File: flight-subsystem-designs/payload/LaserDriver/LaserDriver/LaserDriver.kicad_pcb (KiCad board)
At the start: 4 copper layers, 50.5 x 50 mm, 40 parts, among them J1 Signal In, J2 Laser 0, J3 Laser 1, J5 VIN, U1 74LVC1G04, U2 SY100ELT22ZG-TR, U3 MAX3967AETG+, U4 MAX3967AETG+, U5 LDL212PV33R

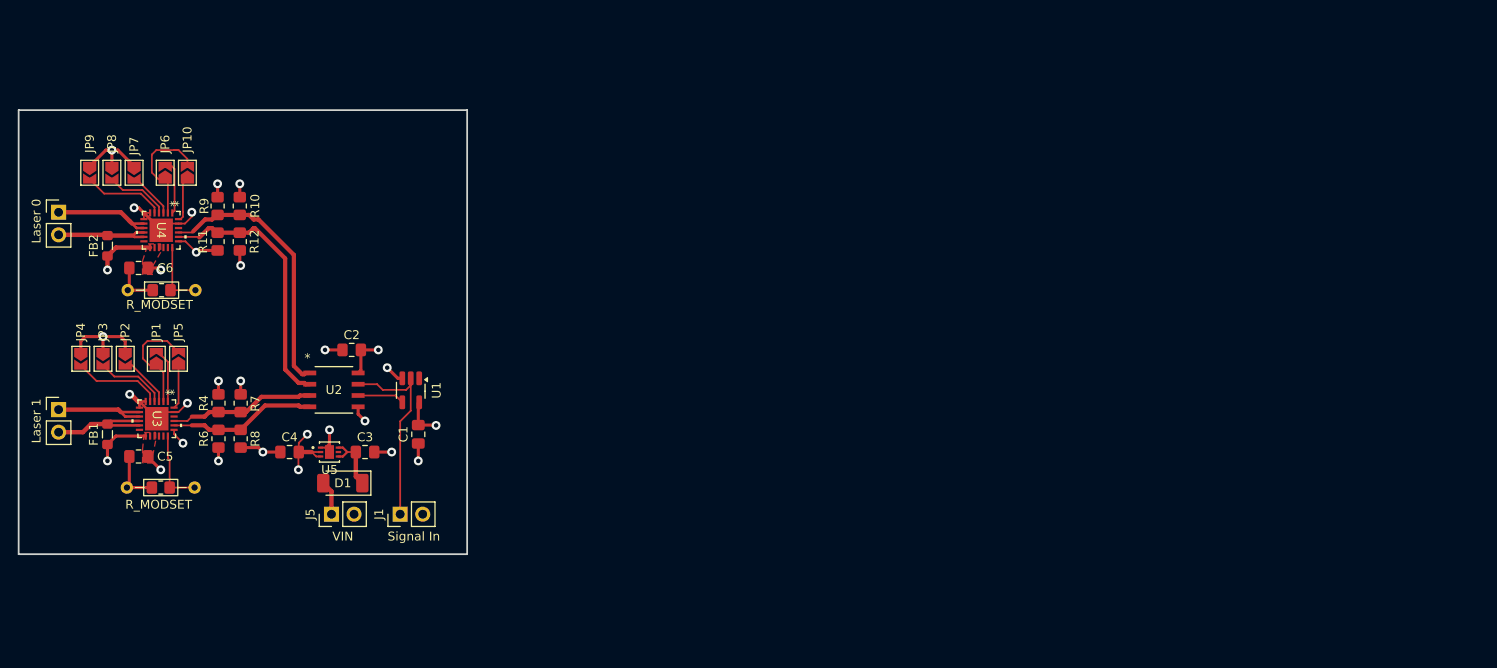
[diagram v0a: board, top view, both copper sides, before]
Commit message: laserdriver: add bnc and mounting holes
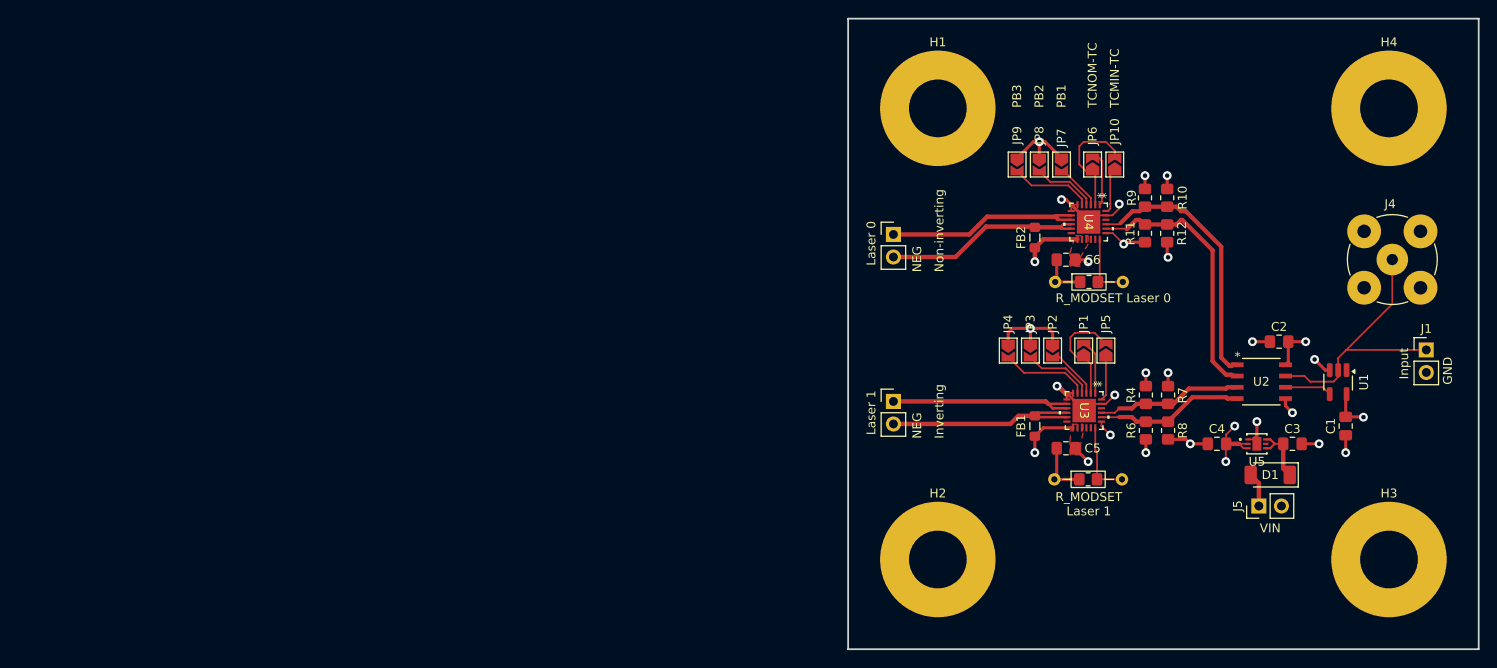
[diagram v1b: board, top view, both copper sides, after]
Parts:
- added H1: MountingHole_Pad, MountingHole:MountingHole_6.5mm_Pad, F.Cu at (127.0, 50.8)
- added H2: MountingHole_Pad, MountingHole:MountingHole_6.5mm_Pad, F.Cu at (127.0, 101.6)
- added H3: MountingHole_Pad, MountingHole:MountingHole_6.5mm_Pad, F.Cu at (177.8, 101.6)
- added H4: MountingHole_Pad, MountingHole:MountingHole_6.5mm_Pad, F.Cu at (177.8, 50.8)
- added J4: BNC, Connector_Coaxial:BNC_TEConnectivity_1478204_Vertical, F.Cu at (178.2, 67.8)
- J1: value Signal In -> Input
- moved J1 117.0 mm to (182.0, 78.0), turned to 0 degrees
- moved C1 104.4 mm to (172.9, 86.6)
- moved C2 104.4 mm to (165.4, 77.1)
- moved C3 104.4 mm to (166.9, 88.6)
- moved C4 104.4 mm to (158.4, 88.6)
- moved C5 104.4 mm to (141.4, 89.1)
- moved C6 104.4 mm to (141.4, 67.8)
- moved D1 104.4 mm to (164.4, 92.1)
- moved FB1 104.4 mm to (137.9, 86.6)
- moved FB2 104.4 mm to (137.9, 65.3)
- moved J5 104.4 mm to (163.2, 95.6)
- moved JP1 104.4 mm to (143.4, 78.1)
- moved JP10 104.4 mm to (146.9, 57.1)
- moved JP2 104.4 mm to (139.9, 78.1)
- moved JP3 104.4 mm to (137.4, 78.1)
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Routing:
- net /Laser0_PWR_N: track 11.1 -> 22.9 mm
- net /Laser0_PWR_P: track 12.1 -> 22.8 mm
- net /Laser1_PWR_N: track 13.3 -> 23.7 mm
- net /Laser1_PWR_P: track 11.5 -> 22.0 mm
- net /SIGNAL_IN: track 22.5 -> 31.2 mm
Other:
- board size 50.5 x 50 mm -> 71 x 71 mm
- board text added: "GND"
- board text added: "Inverting"
- board text added: "NEG"
- board text added: "Non-inverting"
- board text added: "PB1"
- board text added: "PB2"
- board text added: "PB3"
- board text added: "R_MODSET Laser 0"
- board text added: "R_MODSET Laser 1"
- board text added: "TCMIN-TC"
- board text added: "TCNOM-TC"
- board text removed: "R_MODSET"

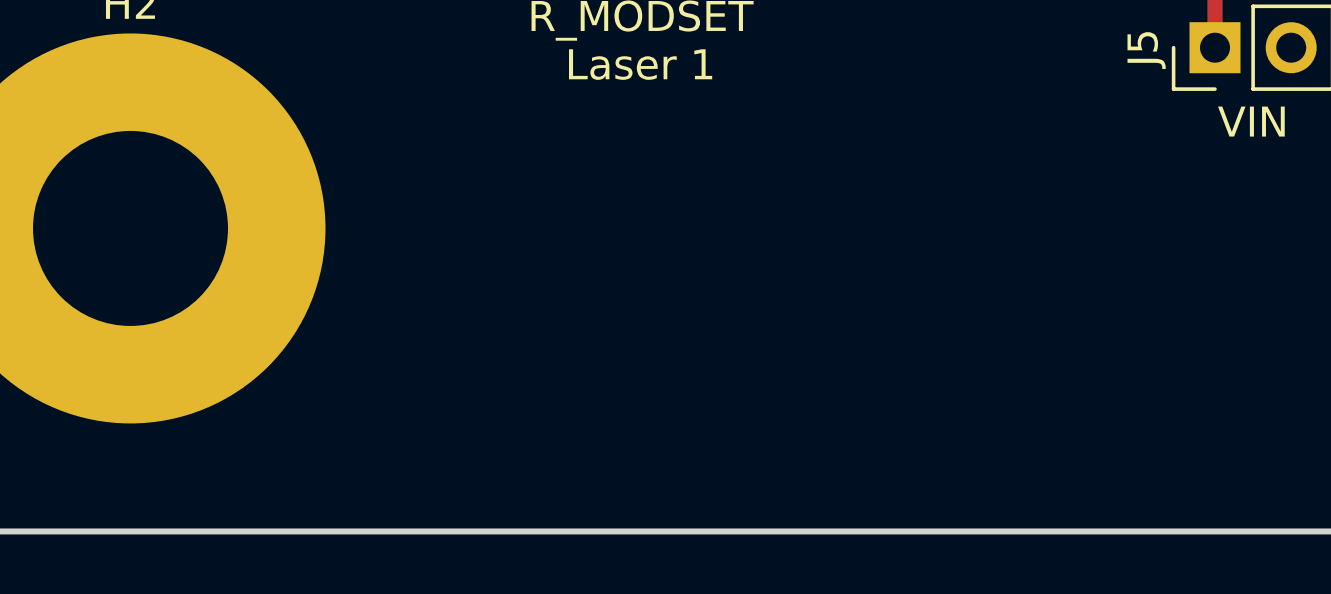
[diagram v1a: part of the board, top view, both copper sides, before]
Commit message: feat: PDU updates and laser driver v1.0.1
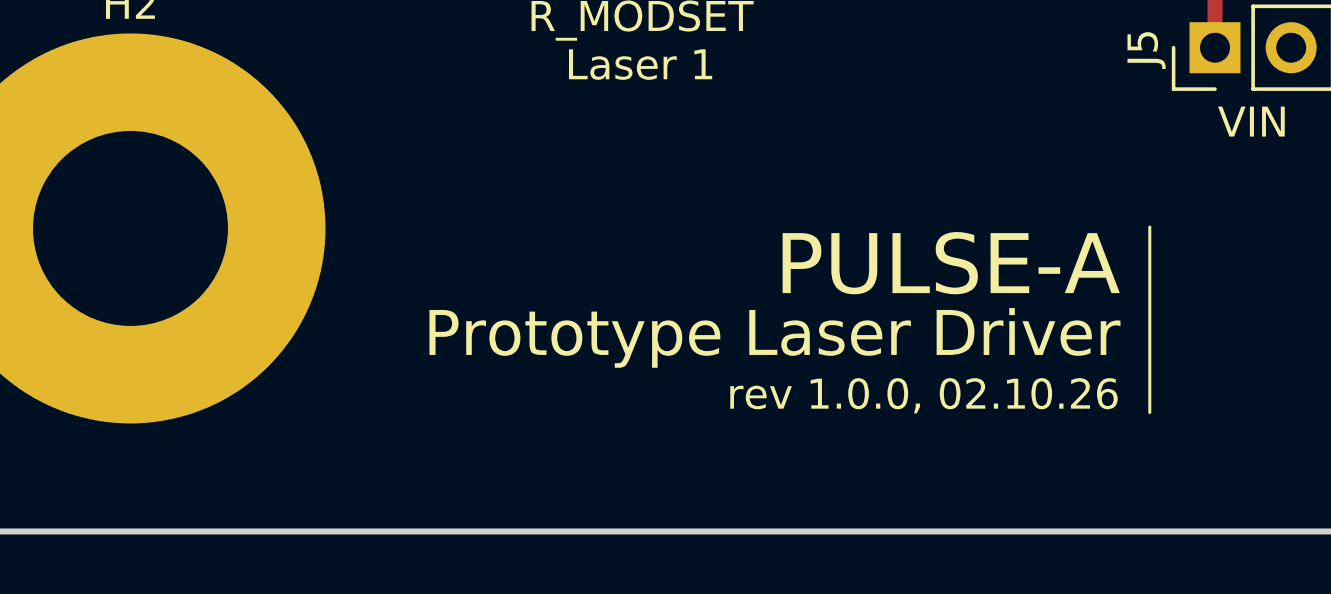
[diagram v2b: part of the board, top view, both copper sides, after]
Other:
- board text added: "PULSE-A"
- board text added: "Prototype Laser Driver"
- board text added: "rev 1.0.0, 02.10.26"

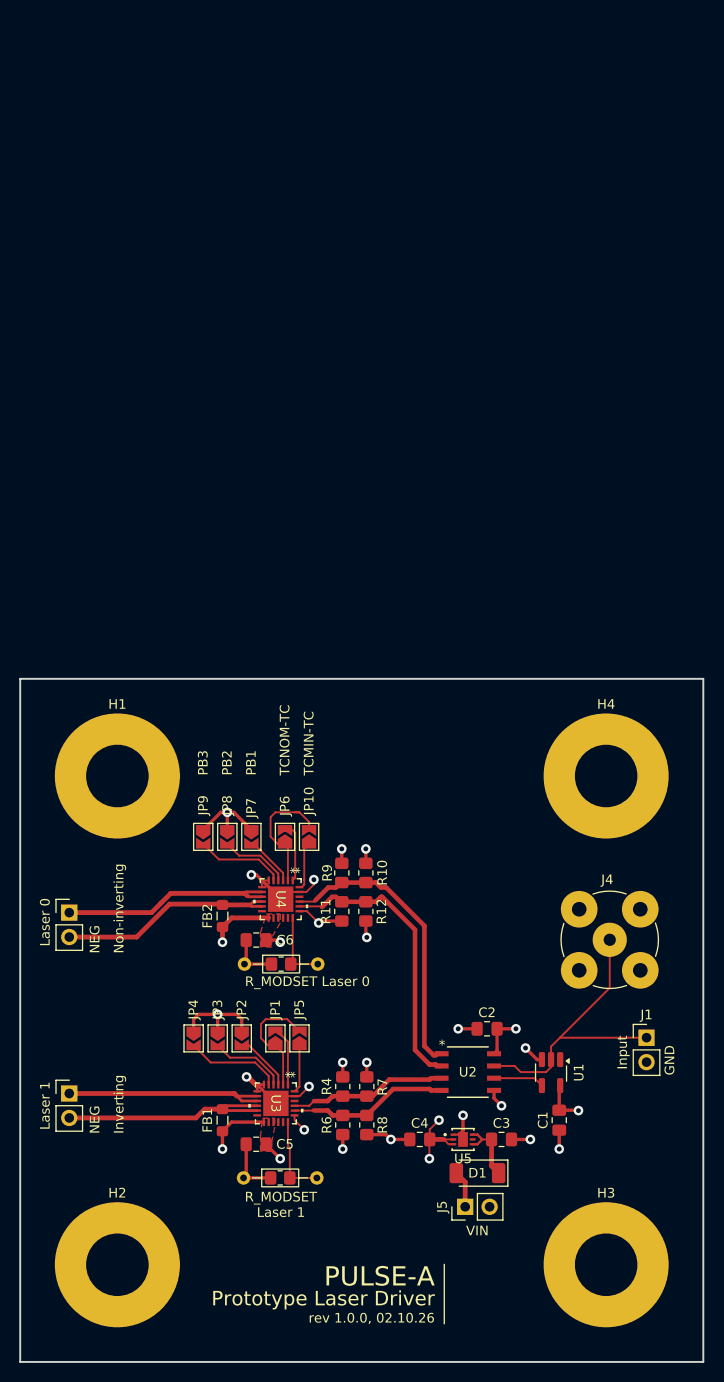
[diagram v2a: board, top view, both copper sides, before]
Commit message: laserdriver: reset all annotations and cleared pcb :sob:
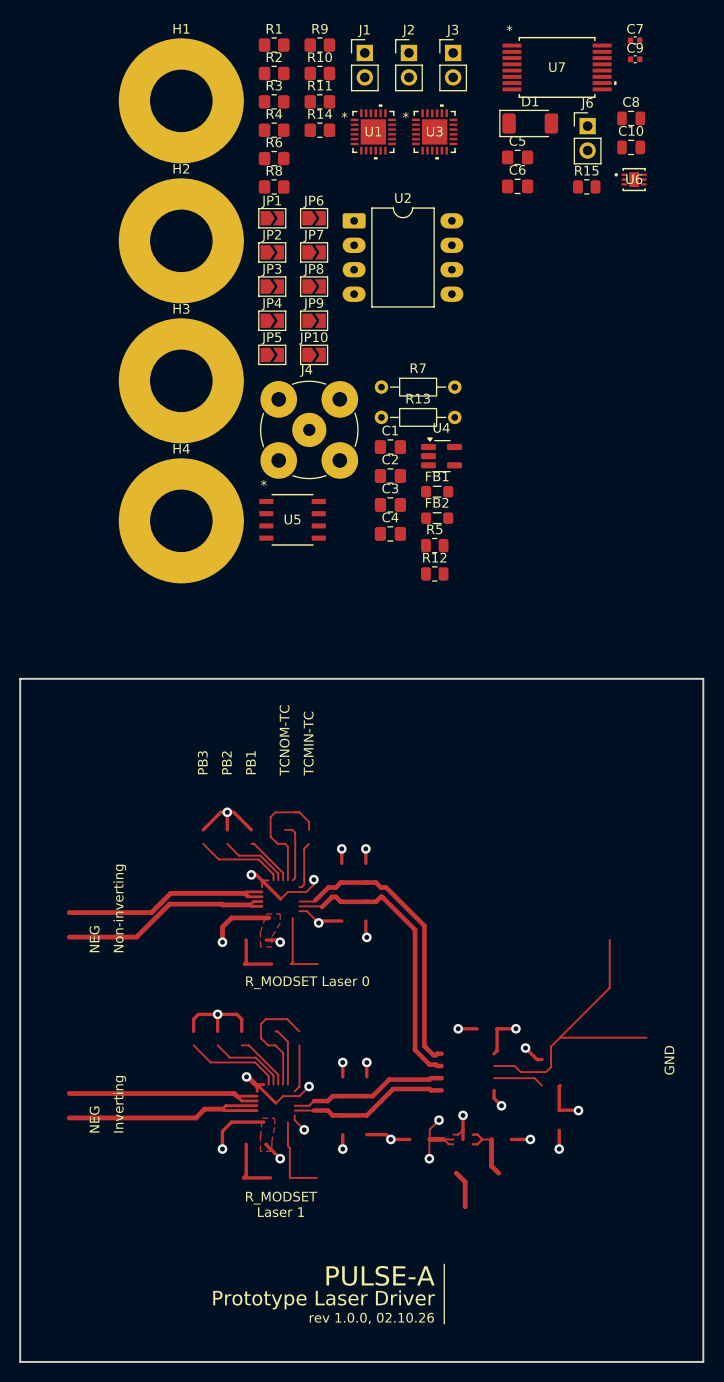
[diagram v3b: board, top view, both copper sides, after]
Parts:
- removed J5: VIN, Connector_PinHeader_2.54mm:PinHeader_1x02_P2.54mm_Vertical
- added C10: 22uF, Capacitor_SMD:C_0805_2012Metric, F.Cu at (180.4, -14.5)
- added C7: 15nF, Capacitor_SMD:C_0402_1005Metric, F.Cu at (180.8, -25.7)
- added C8: 10uF, Capacitor_SMD:C_0805_2012Metric, F.Cu at (180.4, -17.5)
- added C9: 15nF, Capacitor_SMD:C_0402_1005Metric, F.Cu at (180.8, -23.7)
- added J6: VIN Pin Header, Connector_PinHeader_2.54mm:PinHeader_1x02_P2.54mm_Vertical, F.Cu at (175.9, -16.8)
- added R13: R_MODSET, Resistor_THT:R_Axial_DIN0204_L3.6mm_D1.6mm_P7.62mm_Horizontal, F.Cu at (154.4, 13.5)
- added R14: R_MODSET, Resistor_SMD:R_0805_2012Metric_Pad1.20x1.40mm_HandSolder, F.Cu at (148.0, -16.3)
- added R15: 18k, Resistor_SMD:R_0805_2012Metric, F.Cu at (175.8, -10.4)
- added U6: LDL212PV33R, footprints:DFN_V33R_STM, F.Cu at (180.7, -11.2)
- added U7: UCC33420RAQR, footprints:SSOP16_DHA_TEX, F.Cu at (172.7, -22.8)
- C3: value 1uF -> 0.1uF
- C4: value 4.7uF -> 0.1uF
- C5: value 0.1uF -> 4.7uF
- C6: value 0.1uF -> 1uF
- J1: value Input -> Laser 0
- J2: value Laser 0 -> Laser 1
- J3: value Laser 1 -> Input
- R1: value R_MODSET -> 130; footprint Resistor_THT:R_Axial_DIN0204_L3.6mm_D1.6mm_P7.62mm_Horizontal -> Resistor_SMD:R_0805_2012Metric_Pad1.20x1.40mm_HandSolder
- R10, R8: value 83 -> 130
- R11, R4, R9: value 130 -> 83
- R12: value 83 -> 10k; footprint Resistor_SMD:R_0805_2012Metric_Pad1.20x1.40mm_HandSolder -> Resistor_SMD:R_0805_2012Metric
- R2: value R_MODSET -> 83; footprint Resistor_THT:R_Axial_DIN0204_L3.6mm_D1.6mm_P7.62mm_Horizontal -> Resistor_SMD:R_0805_2012Metric_Pad1.20x1.40mm_HandSolder
- R3: value R_MODSET -> 130
- R5: value R_MODSET -> 360; footprint Resistor_SMD:R_0805_2012Metric_Pad1.20x1.40mm_HandSolder -> Resistor_SMD:R_0805_2012Metric
- R6: value 130 -> R_MODSET
- R7: value 83 -> R_MODSET; footprint Resistor_SMD:R_0805_2012Metric_Pad1.20x1.40mm_HandSolder -> Resistor_THT:R_Axial_DIN0204_L3.6mm_D1.6mm_P7.62mm_Horizontal
- U1: value 74LVC1G04 -> MAX3967AETG+; footprint Package_TO_SOT_SMD:SOT-23-5_HandSoldering -> footprints:21-0139_T2444&plus_4_MXM
- U2: value SY100ELT22ZG-TR -> DPC6137; footprint footprints:SOIC-8_M_MCH -> Package_DIP:DIP-8_W10.16mm_LongPads
- U4: value MAX3967AETG+ -> 74LVC1G04; footprint footprints:21-0139_T2444&plus_4_MXM -> Package_TO_SOT_SMD:SOT-23-5_HandSoldering
- U5: value LDL212PV33R -> SY100ELT22ZG-TR; footprint footprints:DFN_V33R_STM -> footprints:SOIC-8_M_MCH
- moved R1 117.8 mm to (143.3, -25.2)
- moved J3 115.3 mm to (161.9, -24.4)
- moved D1 109.2 mm to (169.9, -17.0), turned to 0 degrees
- moved H2 106.6 mm to (133.6, -4.82)
- moved J1 106.5 mm to (152.7, -24.4)
- moved C5 106.1 mm to (168.6, -13.5), turned to 0 degrees
- moved U3 102.3 mm to (160.0, -16.1), turned to 0 degrees
- moved H3 101.9 mm to (133.6, 9.73)
- moved R6 100.7 mm to (143.3, -13.4), turned to 0 degrees
- moved R4 99.7 mm to (143.3, -16.3), turned to 0 degrees
- moved U1 99.5 mm to (153.6, -16.1), turned to 0 degrees
- moved R8 98.0 mm to (143.3, -10.4), turned to 0 degrees
- moved J2 96.1 mm to (157.3, -24.4)
- moved R2 92.6 mm to (143.3, -22.2)
- moved R3 89.6 mm to (143.3, -19.3)
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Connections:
- C1 pad 1: GND -> +3V3
- C1 pad 2: +3V3 -> GND
- C3 pad 1: /VIN -> +3V3
- C6 pad 1: +3V3 -> +5V
- D1 pad 1: /VIN -> /Power Input and Filtering/VIN
- J1 pad 1: /SIGNAL_IN -> /Laser0_PWR_P
- J1 pad 2: GND -> /Laser0_PWR_N
- J2 pad 1: /Laser0_PWR_P -> /Laser1_PWR_P
- J2 pad 2: /Laser0_PWR_N -> /Laser1_PWR_N
- J3 pad 1: /Laser1_PWR_P -> /SIGNAL_IN
- J3 pad 2: /Laser1_PWR_N -> GND
- JP10 pad 1: Net-(JP10-A) -> GND
- JP2 pad 1: GND -> Net-(JP1-A)
- JP5 pad 1: Net-(JP5-A) -> GND
- JP5 pad 2: Net-(JP1-A) -> Net-(JP5-B)
- JP6 pad 1: Net-(JP10-B) -> Net-(JP6-A)
- JP7 pad 1: GND -> Net-(JP6-A)
- R1 pad 1: GND -> +3V3
- R1 pad 2: Net-(U3-MODSET) -> /Laser1_PECL_P
- R10 pad 1: /Laser0_PECL_P -> +3V3
- R10 pad 2: GND -> /Laser0_PECL_N
- R11 pad 1: +3V3 -> /Laser0_PECL_N
- R11 pad 2: /Laser0_PECL_N -> GND
- R12 pad 1: /Laser0_PECL_N -> /ISO_SIGNAL_IN
- R12 pad 2: GND -> +5V
- R2 pad 1: GND -> /Laser1_PECL_P
- R2 pad 2: Net-(U4-MODSET) -> GND
- R3 pad 1: GND -> +3V3
- R3 pad 2: Net-(U4-MODSET) -> /Laser1_PECL_N
- R4 pad 1: +3V3 -> /Laser1_PECL_N
- R4 pad 2: /Laser1_PECL_P -> GND
- R5 pad 2: Net-(U3-MODSET) -> Net-(U2-Cathode)
- R6 pad 1: +3V3 -> Net-(U1-MODSET)
- R6 pad 2: /Laser1_PECL_N -> GND
- R7 pad 1: /Laser1_PECL_P -> Net-(U1-MODSET)
- R8 pad 1: /Laser1_PECL_N -> +3V3
- R8 pad 2: GND -> /Laser0_PECL_P
- R9 pad 1: +3V3 -> /Laser0_PECL_P
- R9 pad 2: /Laser0_PECL_P -> GND
- U1 pad 1: unconnected-(U1-NC-Pad1) -> Net-(JP2-B)
- U1 pad 2: /SIGNAL_IN -> Net-(JP1-A)
- U1 pad 3: GND -> Net-(JP3-B)
- U1 pad 4: Net-(U2-D1) -> Net-(JP4-B)
- U1 pad 5: +3V3 -> Net-(JP5-B)
- U2 pad 1: /Laser0_PECL_P -> unconnected-(U2-NC-Pad1)
- U2 pad 2: /Laser0_PECL_N -> /SIGNAL_IN
- U2 pad 3: /Laser1_PECL_P -> Net-(U2-Cathode)
- U2 pad 4: /Laser1_PECL_N -> unconnected-(U2-NC-Pad4)
- U2 pad 6: Net-(U2-D1) -> /ISO_SIGNAL_IN
- U2 pad 7: /SIGNAL_IN -> +5V
- U2 pad 8: +3V3 -> +5V
- U3 pad 1: Net-(JP1-B) -> Net-(JP7-B)
- U3 pad 10: /Laser1_PWR_N -> /Laser0_PWR_N
- U3 pad 11: /Laser1_PWR_N -> /Laser0_PWR_N
- U3 pad 2: Net-(JP1-A) -> Net-(JP6-A)
- U3 pad 20: /Laser1_PECL_N -> /Laser0_PECL_N
- U3 pad 21: /Laser1_PECL_P -> /Laser0_PECL_P
- U3 pad 24: Net-(JP5-A) -> Net-(JP6-B)
- U3 pad 3: Net-(JP2-B) -> Net-(JP8-B)
- U3 pad 4: Net-(JP3-B) -> Net-(JP9-B)
- U3 pad 5: Net-(JP4-B) -> Net-(JP10-B)
- U3 pad 8: /Laser1_PWR_P -> /Laser0_PWR_P
- U3 pad 9: /Laser1_PWR_P -> /Laser0_PWR_P
- U4 pad 1: Net-(JP6-B) -> unconnected-(U4-NC-Pad1)
- U4 pad 2: Net-(JP10-B) -> /ISO_SIGNAL_IN
- U4 pad 3: Net-(JP7-B) -> GND
- U4 pad 4: Net-(JP8-B) -> Net-(U5-D1)
- U4 pad 5: Net-(JP9-B) -> +3V3
- U5 pad 1: GND -> /Laser0_PECL_P
- U5 pad 2: +3V3 -> /Laser0_PECL_N
- U5 pad 3: +3V3 -> /Laser1_PECL_P
- U5 pad 4: /VIN -> /Laser1_PECL_N
- U5 pad 5: unconnected-(U5-NC-Pad5) -> GND
- U5 pad 6: /VIN -> Net-(U5-D1)
- U5 pad 7: GND -> /SIGNAL_IN
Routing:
- net (no net): track 0.00 -> 30.2 mm
- net Net-(U4-MODSET): track 7.70 -> 0.00 mm
- net /VIN: track 7.18 -> 0.00 mm
- net Net-(U2-D1): track 5.29 -> 0.00 mm
- net Net-(JP10-A): track 5.05 -> 0.00 mm
- net Net-(JP5-A): track 4.98 -> 0.00 mm

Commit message: laserdriver: well f****
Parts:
- moved J3 104.2 mm to (182.0, 77.9)
- moved H3 92.1 mm to (127.0, 101.6)
- moved H4 89.0 mm to (177.8, 101.6)
- moved H2 71.0 mm to (177.8, 50.8)
- moved H1 70.5 mm to (127.0, 50.8)
- moved J4 61.5 mm to (178.2, 67.8)
- moved U3 56.2 mm to (131.9, 32.5)
- moved U2 38.1 mm to (181.1, 17.2)
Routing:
- net GND: track 75.5 -> 0.00 mm, vias 16 -> 0
- net +3V3: track 45.8 -> 0.00 mm, vias 13 -> 0
- net /SIGNAL_IN: track 31.2 -> 0.00 mm
- net /Laser0_PECL_P: track 30.4 -> 0.00 mm
- net /Laser0_PECL_N: track 30.3 -> 0.00 mm
- net (no net): track 30.2 -> 0.00 mm
- net /Laser1_PWR_N: track 23.7 -> 0.00 mm
- net /Laser0_PWR_N: track 22.9 -> 0.00 mm
- net /Laser0_PWR_P: track 22.8 -> 0.00 mm
- net /Laser1_PWR_P: track 22.0 -> 0.00 mm
- net /Laser1_PECL_N: track 16.7 -> 0.00 mm
- net /Laser1_PECL_P: track 16.5 -> 0.00 mm
- net Net-(JP10-B): track 13.7 -> 0.00 mm
- net Net-(JP1-A): track 12.4 -> 0.00 mm
- net Net-(JP4-B): track 10.0 -> 0.00 mm
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- removed copper zone on F.Cu, net +3V3
